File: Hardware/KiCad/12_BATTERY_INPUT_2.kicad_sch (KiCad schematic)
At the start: 0 parts

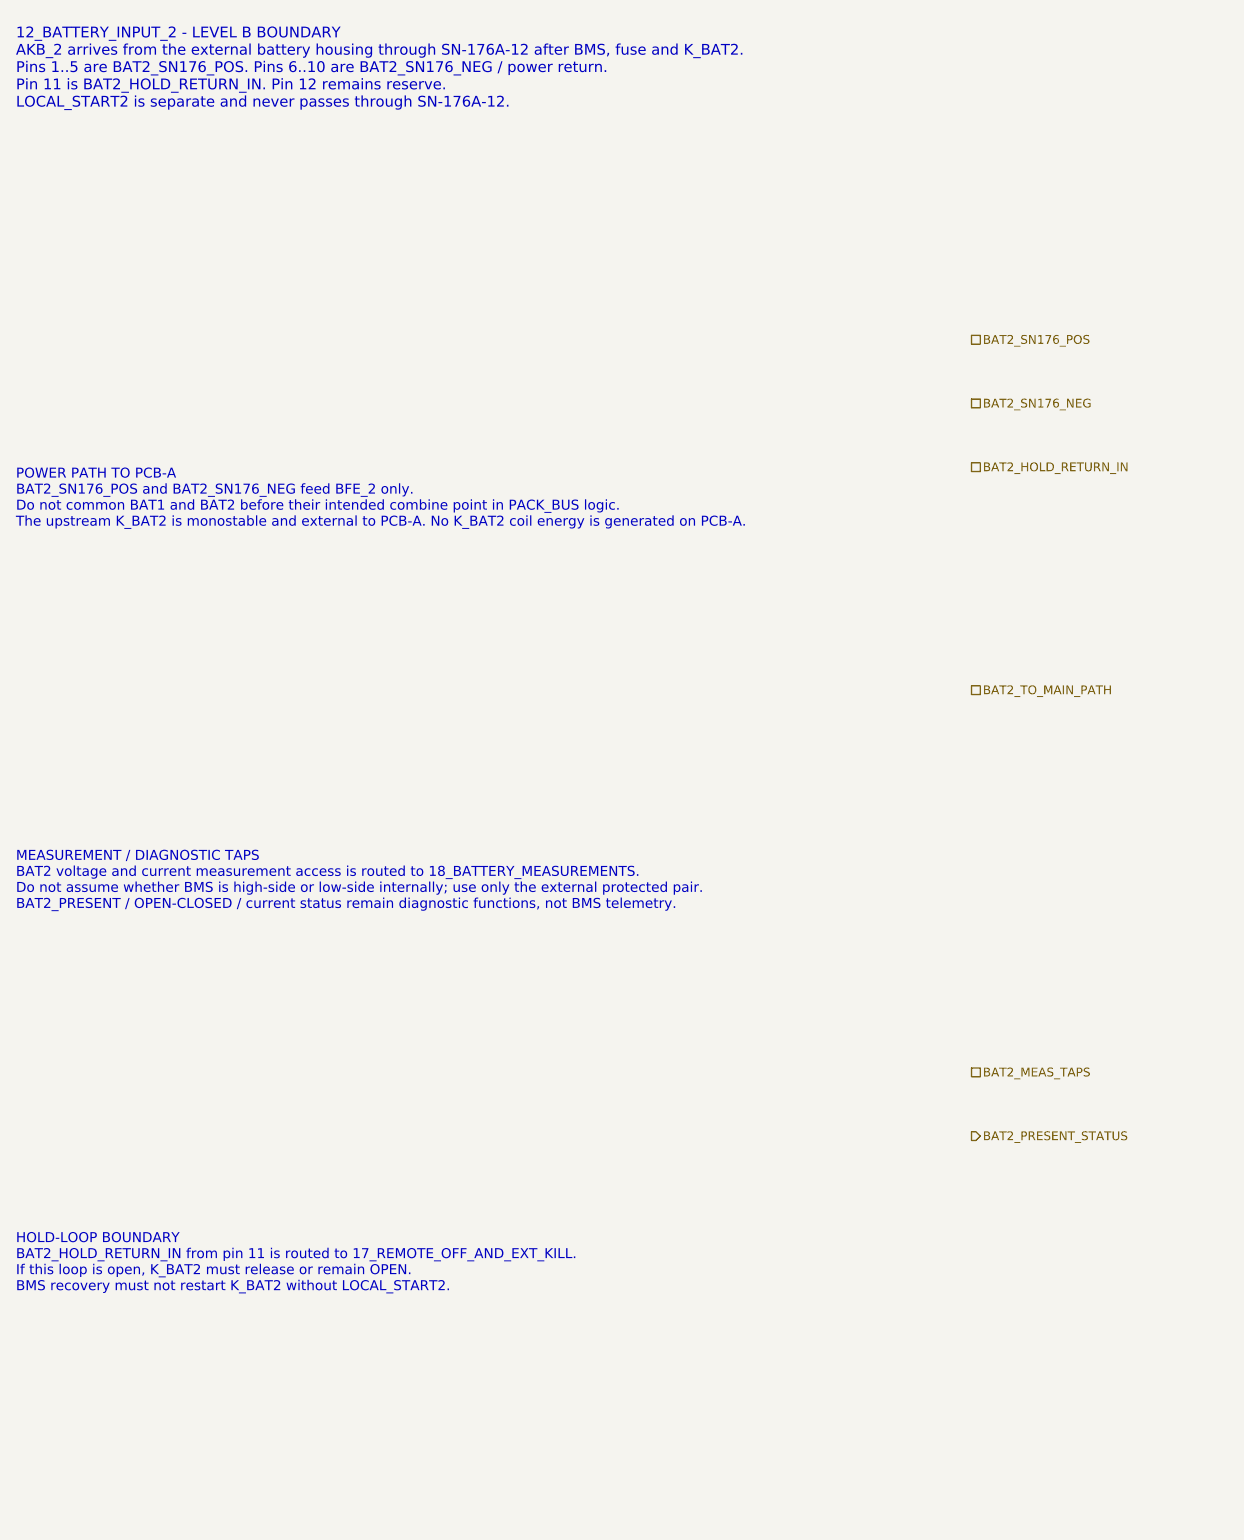
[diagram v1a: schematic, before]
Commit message: hardware: add BFE input and hold-loop symbol skeleton zones
Adds text-only symbol skeleton zones for SN-176A-12 battery input boundaries and hold-loop NC actuator placeholders.

No real KiCad library symbols, footprints, part numbers, PCB layout, or component technology selections are introduced.
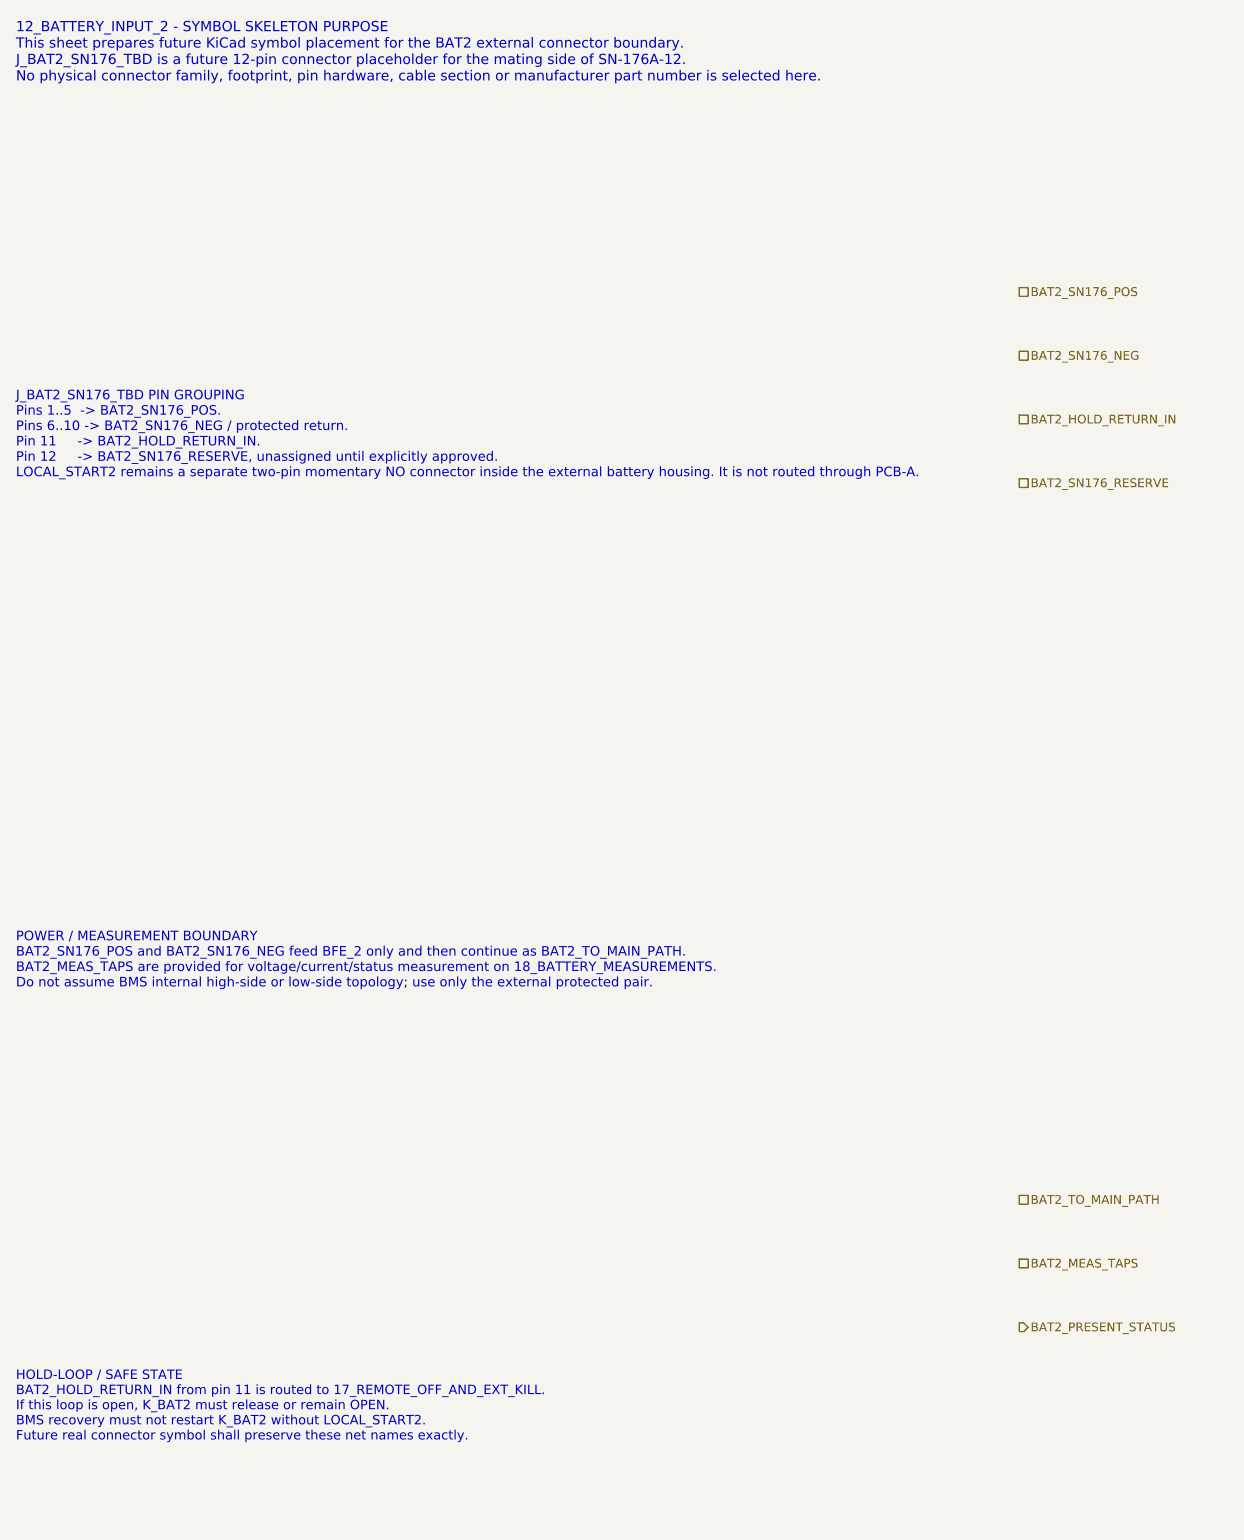
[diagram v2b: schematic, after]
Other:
- note added: "12_BATTERY_INPUT_2 - SYMBOL SKELETON PURPOSE This sheet prepares future KiCad symbol placement for the BAT2 external connector boundary. J_BAT2_SN176_TBD is a future 12-pin connector placeholder for the mating side of SN-176A-12. No physical connector family, footprint, pin hardware, cable section or manufacturer part number is selected here."
- note added: "HOLD-LOOP / SAFE STATE BAT2_HOLD_RETURN_IN from pin 11 is routed to 17_REMOTE_OFF_AND_EXT_KILL. If this loop is open, K_BAT2 must release or remain OPEN. BMS recovery must not restart K_BAT2 without LOCAL_START2. Future real connector symbol shall preserve these net names exactly."
- note added: "J_BAT2_SN176_TBD PIN GROUPING Pins 1..5 -> BAT2_SN176_POS. Pins 6..10 -> BAT2_SN176_NEG / protected return. Pin 11 -> BAT2_HOLD_RETURN_IN. Pin 12 -> BAT2_SN176_RESERVE, unassigned until explicitly approved. LOCAL_START2 remains a separate two-pin momentary NO connector inside the external battery housing. It is not routed through PCB-A."
- note added: "POWER / MEASUREMENT BOUNDARY BAT2_SN176_POS and BAT2_SN176_NEG feed BFE_2 only and then continue as BAT2_TO_MAIN_PATH. BAT2_MEAS_TAPS are provided for voltage/current/status measurement on 18_BATTERY_MEASUREMENTS. Do not assume BMS internal high-side or low-side topology; use only the external protected pair."
- note removed: "12_BATTERY_INPUT_2 - LEVEL B BOUNDARY AKB_2 arrives from the external battery housing through SN-176A-12 after BMS, fuse and K_BAT2. Pins 1..5 are BAT2_SN176_POS. Pins 6..10 are BAT2_SN176_NEG / power return. Pin 11 is BAT2_HOLD_RETURN_IN. Pin 12 remains reserve. LOCAL_START2 is separate and never passes through SN-176A-12."
- note removed: "HOLD-LOOP BOUNDARY BAT2_HOLD_RETURN_IN from pin 11 is routed to 17_REMOTE_OFF_AND_EXT_KILL. If this loop is open, K_BAT2 must release or remain OPEN. BMS recovery must not restart K_BAT2 without LOCAL_START2."
- note removed: "MEASUREMENT / DIAGNOSTIC TAPS BAT2 voltage and current measurement access is routed to 18_BATTERY_MEASUREMENTS. Do not assume whether BMS is high-side or low-side internally; use only the external protected pair. BAT2_PRESENT / OPEN-CLOSED / current status remain diagnostic functions, not BMS telemetry."
- note removed: "POWER PATH TO PCB-A BAT2_SN176_POS and BAT2_SN176_NEG feed BFE_2 only. Do not common BAT1 and BAT2 before their intended combine point in PACK_BUS logic. The upstream K_BAT2 is monostable and external to PCB-A. No K_BAT2 coil energy is generated on PCB-A."
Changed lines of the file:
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@@
 		(title "12_BATTERY_INPUT_2 - BFE input from AKB_2")
 		(date "2026-07-15")
-		(rev "B1")
+		(rev "C0")
 		(company "Gonoboben/plataVM")
-		(comment 1 "Architecture Level B: BAT2 connector boundary and net naming")
-		(comment 2 "Symmetric to 11_BATTERY_INPUT_1")
+		(comment 1 "Symbol skeleton: BAT2 SN-176A-12 boundary and future connector placement zones")
+		(comment 2 "Symmetric to 11_BATTERY_INPUT_1; no connector family or footprint selected")
 	)
-	(text "12_BATTERY_INPUT_2 - LEVEL B BOUNDARY\nAKB_2 arrives from the external battery housing through SN-176A-12 after BMS, fuse and K_BAT2.\nPins 1..5 are BAT2_SN176_POS. Pins 6..10 are BAT2_SN176_NEG / power return.\nPin 11 is BAT2_HOLD_RETURN_IN. Pin 12 remains reserve.\nLOCAL_START2 is separate and never passes through SN-176A-12."
+	(text "12_BATTERY_INPUT_2 - SYMBOL SKELETON PURPOSE\nThis sheet prepares future KiCad symbol placement for the BAT2 external connector boundary.\nJ_BAT2_SN176_TBD is a future 12-pin connector placeholder for the mating side of SN-176A-12.\nNo physical connector family, footprint, pin hardware, cable section or manufacturer part number is selected here."
 		(exclude_from_sim no)
-		(at 12 16 0)
-		(effects (font (size 1.35 1.35)) (justify left))
-		(uuid "bfe-dh-00000012-0000-4000-8000-000000000101")
+		(at 12 14 0)
+		(effects (font (size 1.28 1.28)) (justify left))
+		(uuid "bfe-symbol-00000012-0000-4000-8000-000000000101")
 	)
-	(text "POWER PATH TO PCB-A\nBAT2_SN176_POS and BAT2_SN176_NEG feed BFE_2 only.\nDo not common BAT1 and BAT2 before their intended combine point in PACK_BUS logic.\nThe upstream K_BAT2 is monostable and external to PCB-A. No K_BAT2 coil energy is generated on PCB-A."
+	(text "J_BAT2_SN176_TBD PIN GROUPING\nPins 1..5  -> BAT2_SN176_POS.\nPins 6..10 -> BAT2_SN176_NEG / protected return.\nPin 11     -> BAT2_HOLD_RETURN_IN.\nPin 12     -> BAT2_SN176_RESERVE, unassigned until explicitly approved.\nLOCAL_START2 remains a separate two-pin momentary NO connector inside the external battery housing. It is not routed through PCB-A."
 		(exclude_from_sim no)
-		(at 12 70 0)
-		(effects (font (size 1.25 1.25)) (justify left))
-		(uuid "bfe-dh-00000012-0000-4000-8000-000000000102")
+		(at 12 62 0)
+		(effects (font (size 1.20 1.20)) (justify left))
+		(uuid "bfe-symbol-00000012-0000-4000-8000-000000000102")
 	)
-	(text "MEASUREMENT / DIAGNOSTIC TAPS\nBAT2 voltage and current measurement access is routed to 18_BATTERY_MEASUREMENTS.\nDo not assume whether BMS is high-side or low-side internally; use only the external protected pair.\nBAT2_PRESENT / OPEN-CLOSED / current status remain diagnostic functions, not BMS telemetry."
+	(text "POWER / MEASUREMENT BOUNDARY\nBAT2_SN176_POS and BAT2_SN176_NEG feed BFE_2 only and then continue as BAT2_TO_MAIN_PATH.\nBAT2_MEAS_TAPS are provided for voltage/current/status measurement on 18_BATTERY_MEASUREMENTS.\nDo not assume BMS internal high-side or low-side topology; use only the external protected pair."
 		(exclude_from_sim no)
-		(at 12 118 0)
-		(effects (font (size 1.25 1.25)) (justify left))
-		(uuid "bfe-dh-00000012-0000-4000-8000-000000000103")
+		(at 12 128 0)
+		(effects (font (size 1.20 1.20)) (justify left))
+		(uuid "bfe-symbol-00000012-0000-4000-8000-000000000103")
 	)
-	(text "HOLD-LOOP BOUNDARY\nBAT2_HOLD_RETURN_IN from pin 11 is routed to 17_REMOTE_OFF_AND_EXT_KILL.\nIf this loop is open, K_BAT2 must release or remain OPEN.\nBMS recovery must not restart K_BAT2 without LOCAL_START2."
+	(text "HOLD-LOOP / SAFE STATE\nBAT2_HOLD_RETURN_IN from pin 11 is routed to 17_REMOTE_OFF_AND_EXT_KILL.\nIf this loop is open, K_BAT2 must release or remain OPEN.\nBMS recovery must not restart K_BAT2 without LOCAL_START2.\nFuture real connector symbol shall preserve these net names exactly."
 		(exclude_from_sim no)
-		(at 12 166 0)
-		(effects (font (size 1.25 1.25)) (justify left))
-		(uuid "bfe-dh-00000012-0000-4000-8000-000000000104")
+		(at 12 184 0)
+		(effects (font (size 1.18 1.18)) (justify left))
+		(uuid "bfe-symbol-00000012-0000-4000-8000-000000000104")
 	)
-	(hierarchical_label "BAT2_SN176_POS" (shape passive) (exclude_from_sim no) (at 132 50 0) (effects (font (size 1.1 1.1)) (justify left)) (uuid "bfe-dh-00000012-0000-4000-8000-000000000201"))
-	(hierarchical_label "BAT2_SN176_NEG" (shape passive) (exclude_from_sim no) (at 132 58 0) (effects (font (size 1.1 1.1)) (justify left)) (uuid "bfe-dh-00000012-0000-4000-8000-000000000202"))
-	(hierarchical_label "BAT2_HOLD_RETURN_IN" (shape passive) (exclude_from_sim no) (at 132 66 0) (effects (font (size 1.1 1.1)) (justify left)) (uuid "bfe-dh-00000012-0000-4000-8000-000000000203"))
-	(hierarchical_label "BAT2_TO_MAIN_PATH" (shape passive) (exclude_from_sim no) (at 132 94 0) (effects (font (size 1.1 1.1)) (justify left)) (uuid "bfe-dh-00000012-0000-4000-8000-000000000204"))
-	(hierarchical_label "BAT2_MEAS_TAPS" (shape passive) (exclude_from_sim no) (at 132 142 0) (effects (font (size 1.1 1.1)) (justify left)) (uuid "bfe-dh-00000012-0000-4000-8000-000000000205"))
-	(hierarchical_label "BAT2_PRESENT_STATUS" (shape output) (exclude_from_sim no) (at 132 150 0) (effects (font (size 1.1 1.1)) (justify left)) (uuid "bfe-dh-00000012-0000-4000-8000-000000000206"))
+	(hierarchical_label "BAT2_SN176_POS" (shape passive) (exclude_from_sim no) (at 138 44 0) (effects (font (size 1.1 1.1)) (justify left)) (uuid "bfe-symbol-00000012-0000-4000-8000-000000000201"))
+	(hierarchical_label "BAT2_SN176_NEG" (shape passive) (exclude_from_sim no) (at 138 52 0) (effects (font (size 1.1 1.1)) (justify left)) (uuid "bfe-symbol-00000012-0000-4000-8000-000000000202"))
+	(hierarchical_label "BAT2_HOLD_RETURN_IN" (shape passive) (exclude_from_sim no) (at 138 60 0) (effects (font (size 1.1 1.1)) (justify left)) (uuid "bfe-symbol-00000012-0000-4000-8000-000000000203"))
+	(hierarchical_label "BAT2_SN176_RESERVE" (shape passive) (exclude_from_sim no) (at 138 68 0) (effects (font (size 1.1 1.1)) (justify left)) (uuid "bfe-symbol-00000012-0000-4000-8000-000000000204"))
+	(hierarchical_label "BAT2_TO_MAIN_PATH" (shape passive) (exclude_from_sim no) (at 138 158 0) (effects (font (size 1.1 1.1)) (justify left)) (uuid "bfe-symbol-00000012-0000-4000-8000-000000000205"))
+	(hierarchical_label "BAT2_MEAS_TAPS" (shape passive) (exclude_from_sim no) (at 138 166 0) (effects (font (size 1.1 1.1)) (justify left)) (uuid "bfe-symbol-00000012-0000-4000-8000-000000000206"))
+	(hierarchical_label "BAT2_PRESENT_STATUS" (shape output) (exclude_from_sim no) (at 138 174 0) (effects (font (size 1.1 1.1)) (justify left)) (uuid "bfe-symbol-00000012-0000-4000-8000-000000000207"))
 )
